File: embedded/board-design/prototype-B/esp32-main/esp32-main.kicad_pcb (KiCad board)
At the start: 2 copper layers, 75 x 135.5 mm, 84 parts, among them J1 Conn_ARM_JTAG_SWD_10, J2 Conn_01x08_Socket, J3 Conn_01x08_Socket, J4 0473460001, J5 Conn_01x02_Socket, J6 Conn_01x02_Socket, J7 Conn_01x03_Socket, Q1 BC817, Q2 BC817, Q3 FDN340P, Q4 FMMT720TA, Q5 FDN340P, Q6 FDN340P, U1 ESP32-WROVER-E, U2 BD48ExxG, U3 FT231XS, U4 TPS61090, U5 LTC4054ES5-4.2

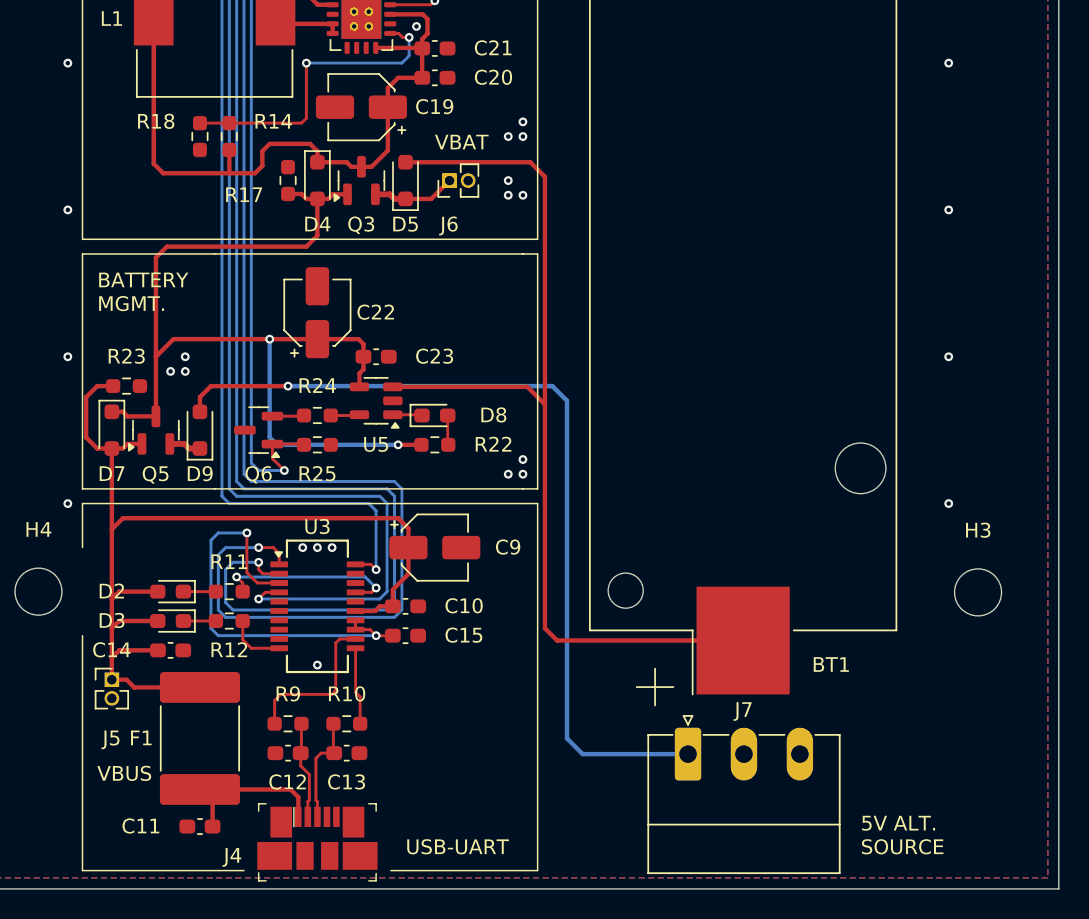
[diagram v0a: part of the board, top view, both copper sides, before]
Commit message: [prototype-B]
Refactored board size and battery switch design. Updated 3D model,
gerber and drill files, and BOM.

Signed-off-by: Nicolae-Andrei Vasile <vasilenicolaeandrei@gmail.com>
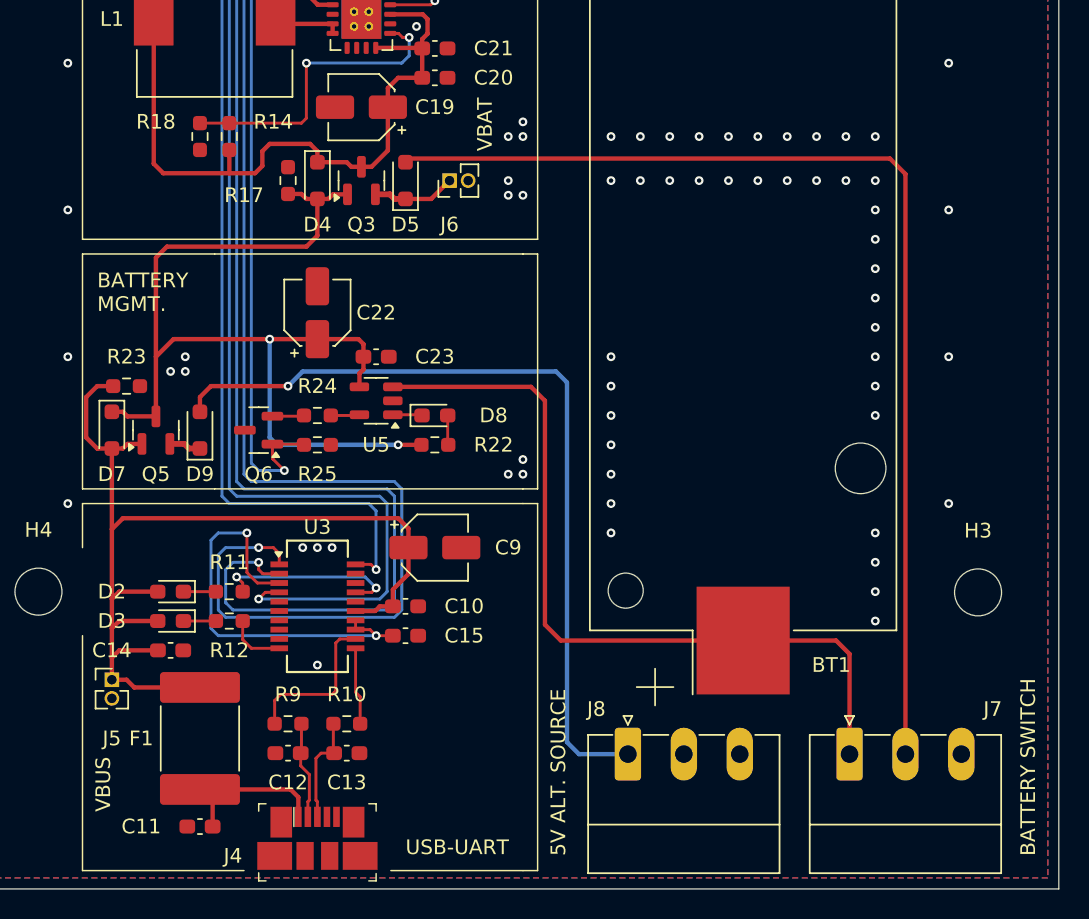
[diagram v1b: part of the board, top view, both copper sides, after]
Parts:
- added J8: Conn_01x03_Socket, Connector_Phoenix_MC:PhoenixContact_MC_1,5_3-G-3.81_1x03_P3.81mm_Horizontal, F.Cu at (153.2, 147.1)
- moved J7 11.0 mm to (168.2, 147.1)
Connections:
- BT1 pad 1: VBAT -> Net-(BT1-+)
- J7 pad 1: /battery/ALT -> Net-(BT1-+)
- J7 pad 2: GND -> VBAT
- U5 pad 3: VBAT -> Net-(BT1-+)
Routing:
- net Net-(BT1-+): track 0.00 -> 54.4 mm
- net VBAT: track 65.4 -> 74.1 mm
- net /battery/ALT: track 58.4 -> 56.0 mm
- net GND: vias 51 -> 90
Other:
- board text added: "BATTERY SWITCH"

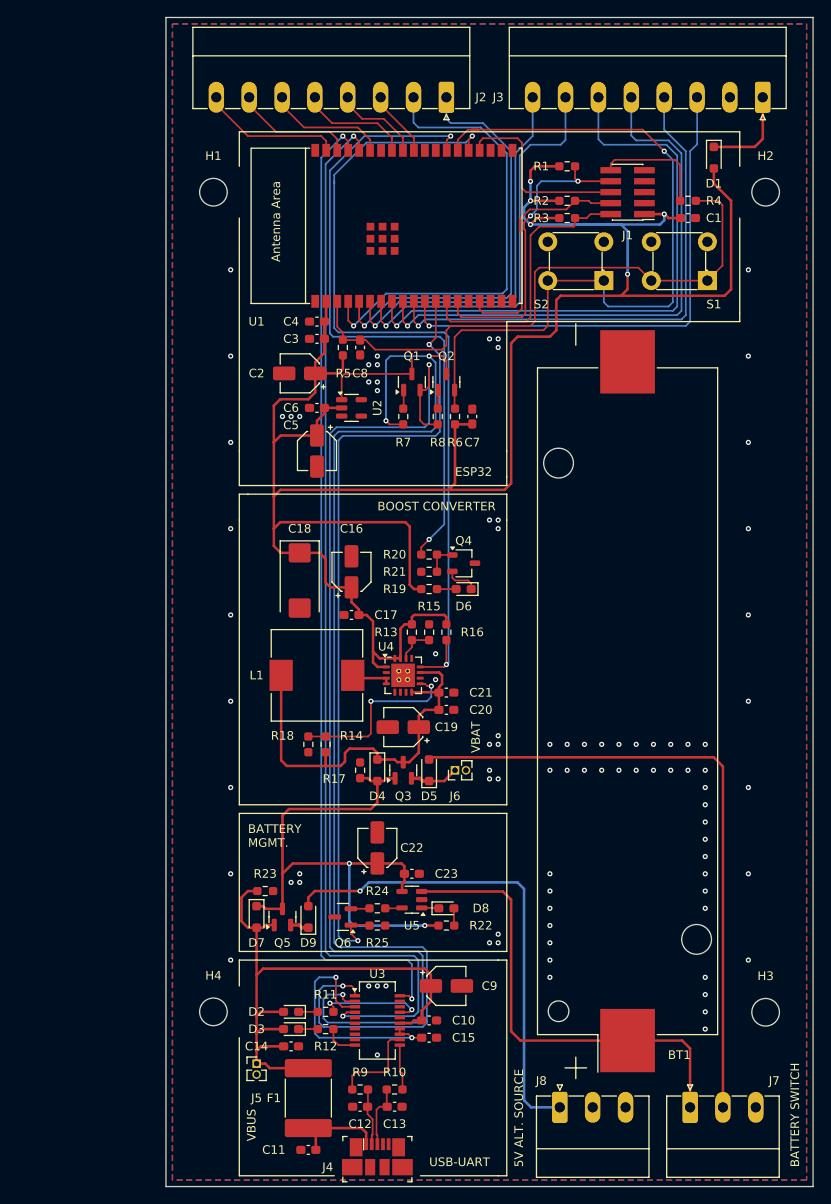
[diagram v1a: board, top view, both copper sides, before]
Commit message: [prototype-B]
Refactored hardware implementation.

Signed-off-by: Nicolae-Andrei Vasile <vasilenicolaeandrei@gmail.com>
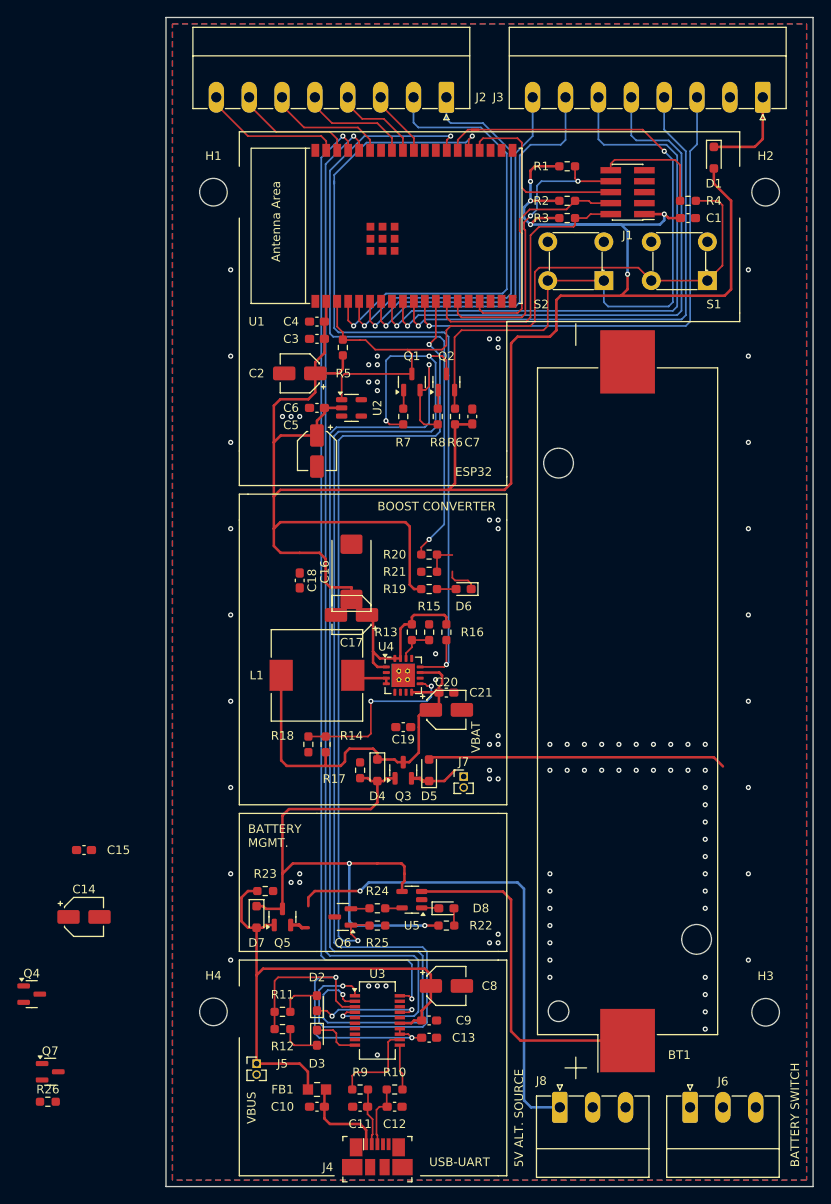
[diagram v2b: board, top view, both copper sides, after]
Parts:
- removed C22: 10uF/16V/20%/4x3mm, Capacitor_SMD:CP_Elec_4x3
- removed C23: 100nF/6.3V/20%/C0603, Capacitor_SMD:C_0603_1608Metric_Pad1.08x0.95mm_HandSolder
- removed D9: SMD22WS-TP, Diode_SMD:D_SOD-323_HandSoldering
- removed F1: SMD050F-2, Fuse:Fuse_2920_7451Metric_Pad2.10x5.45mm_HandSolder
- added FB1: MPZ2012S601AT000, digikey-footprints:0805, F.Cu at (125.0, 145.0)
- added Q7: FDN340P, Package_TO_SOT_SMD:SOT-23, F.Cu at (94.1, 142.9)
- added R26: 10K/R0603, Resistor_SMD:R_0603_1608Metric_Pad0.98x0.95mm_HandSolder, F.Cu at (93.8, 146.4)
- C10: value 100nF/6.3V/20%/C0603 -> 10nF/6.3V/20%/C0603
- C11: value 10nF/6.3V/20%/C0603 -> 47pF/6.3V/20%/C0603
- C13: value 47pF/6.3V/20%/C0603 -> 100nF/6.3V/20%/C0603
- C14, C17: value 10uF/6.3V/20%/C0603 -> 22uF/16V/20%/4x3mm; footprint Capacitor_SMD:C_0603_1608Metric_Pad1.08x0.95mm_HandSolder -> Capacitor_SMD:CP_Elec_4x3
- C15: value 100nF/6.3V/20%/C0603 -> 10uF/6.3V/20%/C0603
- C16: value 22uF/16V/20%/4x3mm -> 220uF/16V/10%/D/Tantalum; footprint Capacitor_SMD:CP_Elec_4x3 -> Capacitor_Tantalum_SMD:CP_EIA-7343-31_Kemet-D_Pad2.25x2.55mm_HandSolder
- C18: value 220uF/16V/10%/D/Tantalum -> 10uF/6.3V/20%/C0603; footprint Capacitor_Tantalum_SMD:CP_EIA-7343-31_Kemet-D_Pad2.25x2.55mm_HandSolder -> Capacitor_SMD:C_0603_1608Metric_Pad1.08x0.95mm_HandSolder
- C19: value 22uF/16V/20%/4x3mm -> 100nF/6.3V/20%/C0603; footprint Capacitor_SMD:CP_Elec_4x3 -> Capacitor_SMD:C_0603_1608Metric_Pad1.08x0.95mm_HandSolder
- C20: value 10uF/6.3V/20%/C0603 -> 10uF/16V/20%/4x3mm; footprint Capacitor_SMD:C_0603_1608Metric_Pad1.08x0.95mm_HandSolder -> Capacitor_SMD:CP_Elec_4x3
- C7: value 10uF/6.3V/20%/C0603 -> 1uF/6.3V/20%/C0603
- C8: value 1uF/6.3V/20%/C0603 -> 10uF/16V/20%/4x3mm; footprint Capacitor_SMD:C_0603_1608Metric_Pad1.08x0.95mm_HandSolder -> Capacitor_SMD:CP_Elec_4x3
- C9: value 10uF/16V/20%/4x3mm -> 100nF/6.3V/20%/C0603; footprint Capacitor_SMD:CP_Elec_4x3 -> Capacitor_SMD:C_0603_1608Metric_Pad1.08x0.95mm_HandSolder
- D2: value LED(GREEN) -> LED(RED)
- D3: value LED(RED) -> LED(GREEN)
- J6: value Conn_01x02_Socket -> Conn_01x03_Socket; footprint Connector_PinHeader_1.27mm:PinHeader_1x02_P1.27mm_Vertical -> Connector_Phoenix_MC:PhoenixContact_MC_1,5_3-G-3.81_1x03_P3.81mm_Horizontal
- J7: value Conn_01x03_Socket -> Conn_01x02_Socket; footprint Connector_Phoenix_MC:PhoenixContact_MC_1,5_3-G-3.81_1x03_P3.81mm_Horizontal -> Connector_PinHeader_1.27mm:PinHeader_1x02_P1.27mm_Vertical
- L1: value CDRH103RNP-2R2NC-B -> CDRH103RNP-8R2NC-B
- Q4: value FMMT720TA -> FDN340P; footprint Package_TO_SOT_SMD:TSOT-23 -> Package_TO_SOT_SMD:SOT-23
- Q5: value FDN340P -> BC807
- R11, R12: value 330R/R0603 -> 270R/R0603
- R14: value 1.8M/R0603 -> 2M/R0603
- R18: value 380K/R0603 -> 100K/R0603
- R19: value 330R/R0603 -> 390K/R0603
- R20: value 1K/R0603 -> 270R/R0603
- R21: value 10K/R0603 -> 1K/R0603
- R22: value 330R/R0603 -> 10K/R0603
- R25: value 10K/R0603 -> 2K/R0603
- moved C8 74.7 mm to (140.0, 133.0), turned to 0 degrees
- moved Q4 70.7 mm to (91.9, 133.9)
- moved J6 47.6 mm to (168.2, 147.1), turned to 0 degrees
- moved J7 46.5 mm to (142.0, 108.7)
- moved C15 45.5 mm to (98.0, 117.2)
- moved C14 28.3 mm to (98.0, 125.0)
- moved C10 16.4 mm to (125.0, 147.0), turned to 180 degrees
- moved C13 8.94 mm to (138.0, 139.0)
- moved C11 7.81 mm to (130.0, 147.0)
- moved R11 5.00 mm to (121.0, 136.0)
- moved R12 5.00 mm to (121.0, 138.0)
- moved C9 4.47 mm to (138.0, 137.0)
- moved C12 4.00 mm to (134.0, 147.0), turned to 0 degrees
- moved D2 3.16 mm to (125.0, 135.0), turned to 90 degrees
- moved D3 3.16 mm to (125.0, 139.0), turned to -90 degrees
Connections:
- BT1 pad 1: Net-(BT1-+) -> VBAT
- C10 pad 1: VBUS -> Net-(C10-Pad1)
- C11 pad 1: Net-(C11-Pad1) -> /usb-uart/D-
- C12 pad 1: /usb-uart/D- -> /usb-uart/D+
- C13 pad 1: /usb-uart/D+ -> Net-(U3-3V3OUT)
- C14 pad 1: VBUS -> +3V3
- C15 pad 1: Net-(U3-3V3OUT) -> +3V3
- C17 pad 1: +3V3 -> Net-(D5-K)
- C18 pad 1: +3V3 -> Net-(D5-K)
- C19 pad 1: Net-(D4-K) -> Net-(D5-K)
- C20 pad 1: Net-(D4-K) -> Net-(D7-K)
- C21 pad 1: Net-(D4-K) -> Net-(D7-K)
- C7 pad 1: +3V3 -> Net-(Q1-C)
- C8 pad 1: Net-(Q1-C) -> VBUS
- D2 pad 2: VBUS -> Net-(D2-A)
- D3 pad 2: VBUS -> Net-(D3-A)
- D4 pad 2: +5V -> ALT
- D5 pad 1: /power-supply/VBAT_TEST -> Net-(D5-K)
- D5 pad 2: VBAT -> VBUS
- D7 pad 1: +5V -> Net-(D7-K)
- D8 pad 2: Net-(D8-A) -> Net-(D7-K)
- J4 pad 1: Net-(C11-Pad1) -> Net-(C10-Pad1)
- J6 pad 1: /power-supply/VBAT_TEST -> Net-(D4-K)
- J6 pad 2: GND -> Net-(J6-Pin_2)
- J7 pad 1: Net-(BT1-+) -> VBAT
- J7 pad 2: VBAT -> GND
- J8 pad 1: /battery/ALT -> ALT
- L1 pad 1: Net-(D4-K) -> Net-(D5-K)
- Q3 pad 1: +5V -> ALT
- Q3 pad 2: /power-supply/VBAT_TEST -> Net-(D4-K)
- Q3 pad 3: Net-(D4-K) -> VBAT
- Q4 pad 1: Net-(Q4-B) -> VBUS
- Q4 pad 2: Net-(D6-K) -> Net-(D5-K)
- Q4 pad 3: GND -> Net-(J6-Pin_2)
- Q5 pad 1: VBUS -> Net-(Q5-B)
- Q5 pad 2: Net-(D9-K) -> Net-(D6-K)
- Q5 pad 3: +5V -> GND
- Q6 pad 1: /battery/~{SHDN} -> VBUS
- Q6 pad 2: Net-(Q6-S) -> Net-(D7-K)
- Q6 pad 3: GND -> ALT
- R11 pad 1: Net-(U3-CBUS1) -> Net-(D2-A)
- R11 pad 2: Net-(D2-K) -> Net-(U3-3V3OUT)
- R12 pad 1: Net-(U3-CBUS2) -> Net-(D3-A)
- R12 pad 2: Net-(D3-K) -> Net-(U3-3V3OUT)
- R14 pad 1: Net-(D4-K) -> Net-(D5-K)
- R17 pad 2: +5V -> ALT
- R18 pad 2: Net-(U4-LBI) -> VBUS
- R19 pad 1: +3V3 -> GND
- R19 pad 2: Net-(D6-A) -> Net-(U4-LBI)
- R20 pad 1: Net-(Q4-B) -> +3V3
- R20 pad 2: /power-supply/PWRLED -> Net-(D6-A)
- R21 pad 1: Net-(Q4-B) -> Net-(Q5-B)
- R21 pad 2: GND -> /power-supply/PWRLED
- R22 pad 1: +5V -> Net-(Q5-B)
- R22 pad 2: Net-(D8-A) -> GND
- R24 pad 1: Net-(U5-PROG) -> Net-(D8-K)
- R24 pad 2: Net-(Q6-S) -> Net-(U5-~{CHRG})
- R25 pad 1: GND -> Net-(U5-PROG)
- R25 pad 2: /battery/~{SHDN} -> Net-(Q7-S)
- U1 pad 12: /battery/~{SHDN} -> /battery/SHDN
- U3 pad 10: Net-(U3-CBUS2) -> Net-(D3-K)
- U3 pad 17: Net-(U3-CBUS1) -> Net-(D2-K)
- U4 pad 11: Net-(D4-K) -> Net-(D5-K)
- U4 pad 8: Net-(D4-K) -> Net-(D5-K)
- U5 pad 1: Net-(D8-K) -> Net-(U5-~{CHRG})
- U5 pad 3: Net-(BT1-+) -> VBAT
- U5 pad 4: +5V -> Net-(D7-K)
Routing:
- net VBUS: track 70.3 -> 189.5 mm, vias 0 -> 2
- net /battery/~{SHDN}: track 92.4 -> 0.00 mm, vias 2 -> 0
- net (no net): track 0.00 -> 79.1 mm
- net +5V: track 67.4 -> 0.00 mm, vias 2 -> 0
- net ALT: track 0.00 -> 56.0 mm, vias 0 -> 1
- net /battery/ALT: track 56.0 -> 0.00 mm, vias 1 -> 0
- net Net-(BT1-+): track 54.4 -> 0.00 mm
- net VBAT: track 74.1 -> 40.0 mm
- net Net-(U3-3V3OUT): track 28.7 -> 41.5 mm
- net Net-(U3-CBUS1): track 12.5 -> 0.00 mm, vias 2 -> 0
- net Net-(C11-Pad1): track 11.1 -> 0.00 mm
- net Net-(D2-K): track 2.21 -> 13.1 mm, vias 0 -> 2
- net Net-(C10-Pad1): track 0.00 -> 10.5 mm
- net /power-supply/VBAT_TEST: track 5.70 -> 0.00 mm
- net Net-(D3-A): track 0.00 -> 4.69 mm
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
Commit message: [prototype-B]
Work in progress - refactoring hardware implementation.

Signed-off-by: Nicolae-Andrei Vasile <vasilenicolaeandrei@gmail.com>
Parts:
- moved Q4 50.3 mm to (135.0, 108.0), turned to -90 degrees
- moved C14 48.4 mm to (128.0, 87.0), turned to -90 degrees
- moved Q5 45.6 mm to (140.9, 84.0), turned to -90 degrees
- moved R22 45.0 mm to (140.9, 81.0), turned to 180 degrees
- moved R26 43.3 mm to (132.0, 126.0), turned to 180 degrees
- moved C15 39.4 mm to (122.0, 86.0), turned to -90 degrees
- moved Q7 38.4 mm to (128.0, 125.0), turned to 180 degrees
- moved C21 21.4 mm to (136.0, 120.0)
- moved C18 20.8 mm to (140.0, 98.0), turned to 0 degrees
- moved R19 18.4 mm to (129.0, 103.0)
- moved C20 17.9 mm to (132.0, 117.0), turned to 90 degrees
- moved C7 15.3 mm to (130.0, 59.0), turned to -90 degrees
- moved R17 15.0 mm to (145.0, 108.0), turned to 90 degrees
- moved R18 14.3 mm to (138.0, 108.0)
- moved C17 11.7 mm to (135.0, 100.0)
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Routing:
- net Net-(J6-Pin_2): track 0.00 -> 93.7 mm, vias 0 -> 1
- net /battery/SHDN: track 0.00 -> 92.4 mm, vias 0 -> 2
- net VBUS: track 189.5 -> 106.9 mm, vias 2 -> 0
- net (no net): track 79.1 -> 0.00 mm
- net Net-(D5-K): track 0.00 -> 49.2 mm
- net Net-(D7-K): track 0.00 -> 48.1 mm, vias 2 -> 0
- net ALT: track 56.0 -> 95.6 mm, vias 1 -> 2
- net Net-(D4-K): track 47.5 -> 86.1 mm
- net VBAT: track 40.0 -> 59.4 mm
- net +3V3: track 264.3 -> 245.0 mm
- net Net-(Q5-B): track 0.00 -> 4.08 mm
- net Net-(D6-K): track 6.01 -> 2.08 mm
- net /power-supply/PWRLED: track 75.8 -> 72.4 mm
- net Net-(Q7-S): track 0.00 -> 2.17 mm
- net GND: track 2.02 -> 0.00 mm, vias 90 -> 96
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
